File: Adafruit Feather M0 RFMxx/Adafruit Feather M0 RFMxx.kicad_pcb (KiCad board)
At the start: 2 copper layers, 50.8 x 22.9 mm, 41 parts, among them SW1 SPST_TACT-KMR2, U1 2MB Flash, U2 AP2112K-3.3, U3 MCP73831T-2ACI/OT, U4 RFM69HCW, X1 JSTPH, X2 32.768, X3 microUSB, X4 uFL

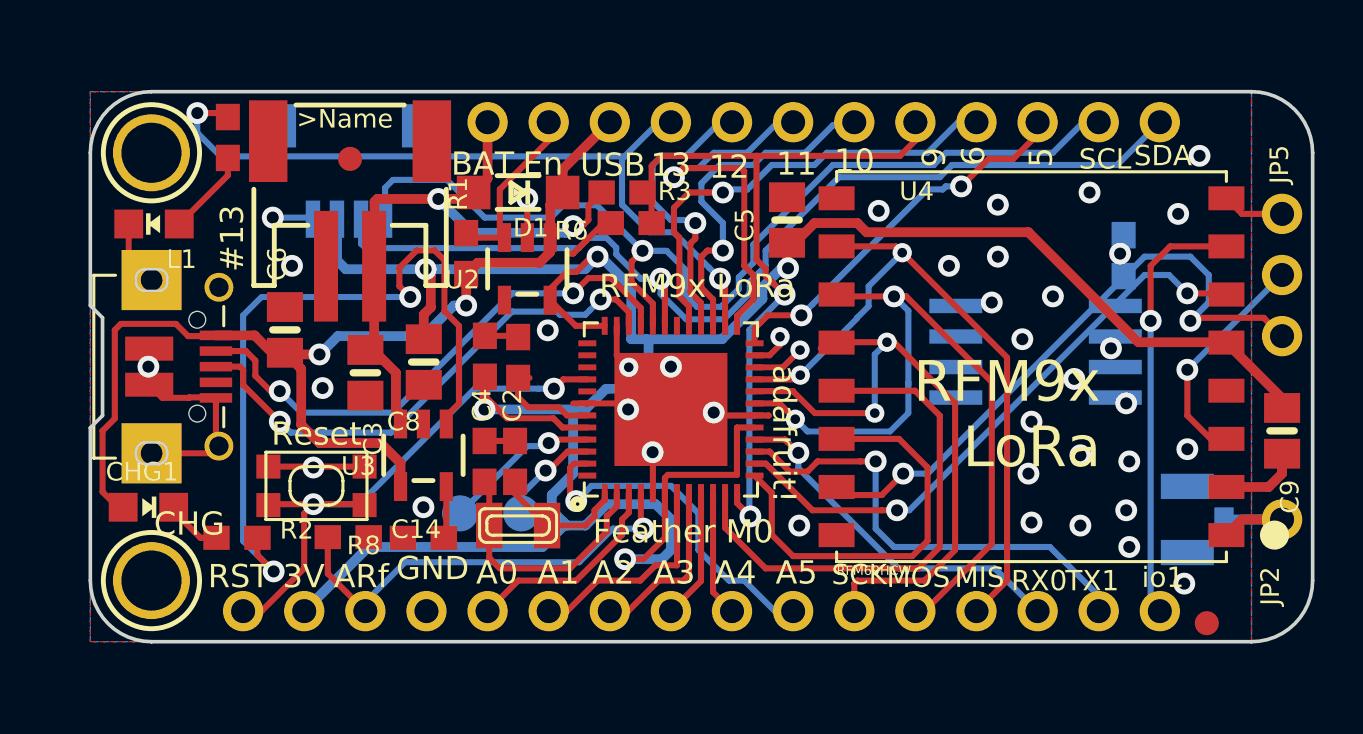
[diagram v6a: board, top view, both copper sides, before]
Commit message: New RST and IRQ lines chosen for RFM. Everything routed. DRC errors still to be fixed.
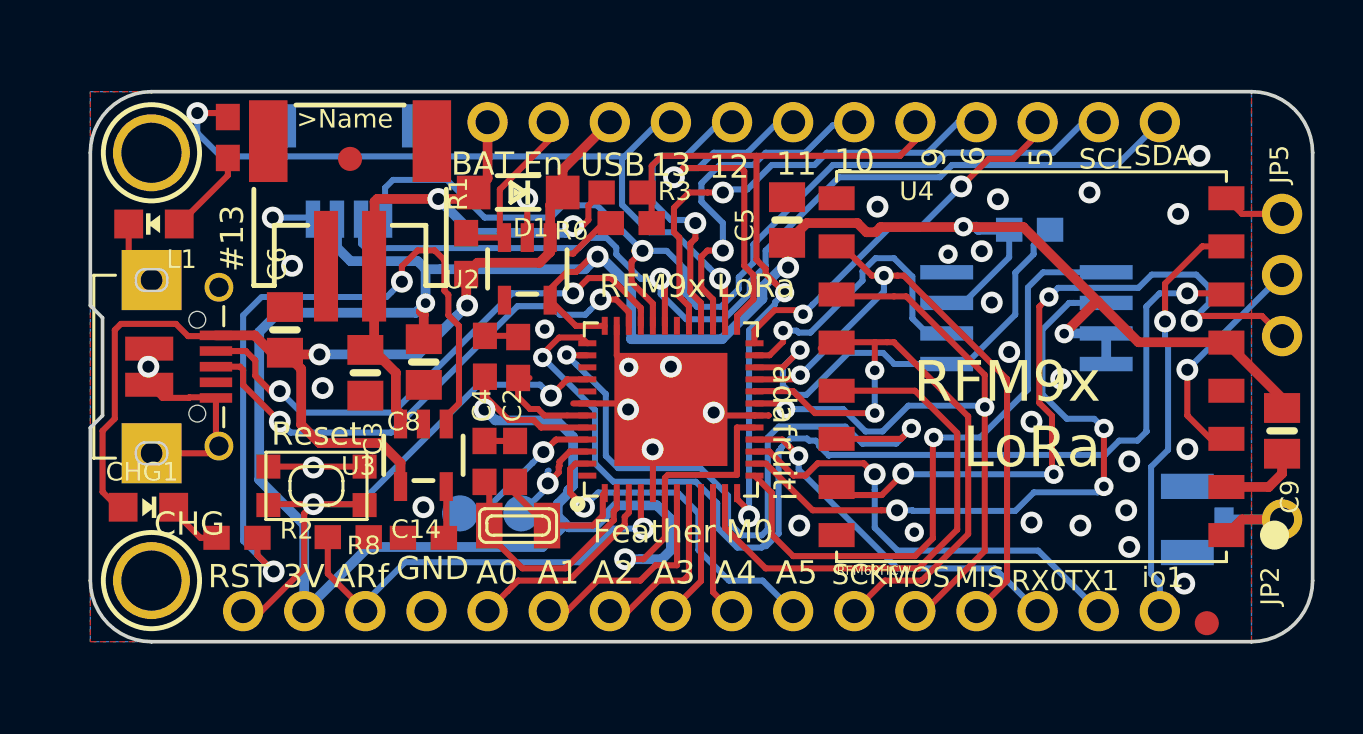
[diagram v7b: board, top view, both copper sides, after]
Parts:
- moved R4 4.05 mm to (162.1, 99.3), turned to 180 degrees
- moved U1 1.45 mm to (162.0, 103.0)
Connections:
- U$4 pad 13: /D4_RST -> /D4_FLASHMOSI
- U$4 pad 14: /D3_IRQ -> /D3_FLASHSCK
- U$4 pad 37: Net-(U$4-Pad37) -> /RXD_IRQ
- U$4 pad 38: Net-(U$4-Pad38) -> /TXD_RST
- U4 pad 14P: /D4_RST -> /TXD_RST
- U4 pad 6P: /D3_IRQ -> /RXD_IRQ
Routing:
- net /RXD_IRQ: track 0.00 -> 46.1 mm, vias 0 -> 2
- net /TXD_RST: track 0.00 -> 28.4 mm, vias 0 -> 2
- net /D4_FLASHMOSI: track 0.00 -> 27.6 mm, vias 0 -> 1
- net /D3_FLASHSCK: track 0.00 -> 27.1 mm, vias 0 -> 3
- net +3V3: track 112.8 -> 137.8 mm, vias 6 -> 7
- net /D3_IRQ: track 24.8 -> 0.00 mm, vias 2 -> 0
- net /FLASH_CS: track 2.19 -> 19.7 mm, vias 2 -> 1
- net /D4_RST: track 17.2 -> 0.00 mm
- net /D2_FLASHMISO: track 1.58 -> 12.5 mm
- net /DIO5: track 26.5 -> 30.5 mm, vias 2 -> 4
- net /MOSI: track 31.6 -> 29.3 mm
- net /MISO: track 28.9 -> 27.1 mm
- net Net-(R2-Pad2): track 31.0 -> 30.1 mm
- net /DIO1: track 18.0 -> 17.3 mm
- net Net-(C4-Pad1): track 10.7 -> 10.1 mm
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
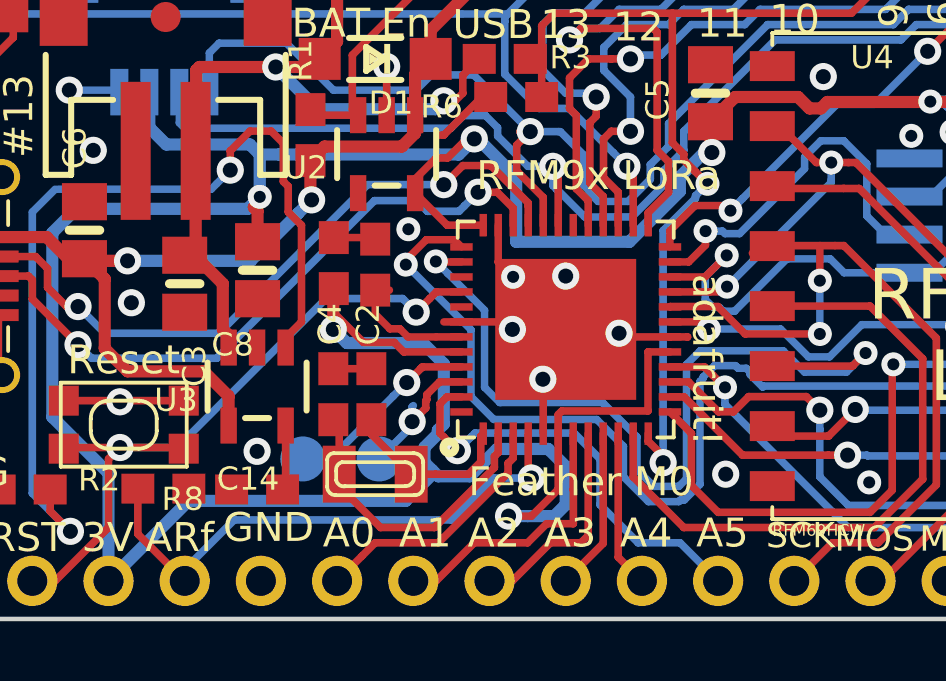
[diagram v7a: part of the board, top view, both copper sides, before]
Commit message: Fixed DRC errors. Remaining are ignores? - 2 pads part of USB connector - Top and Bottom regions not connected
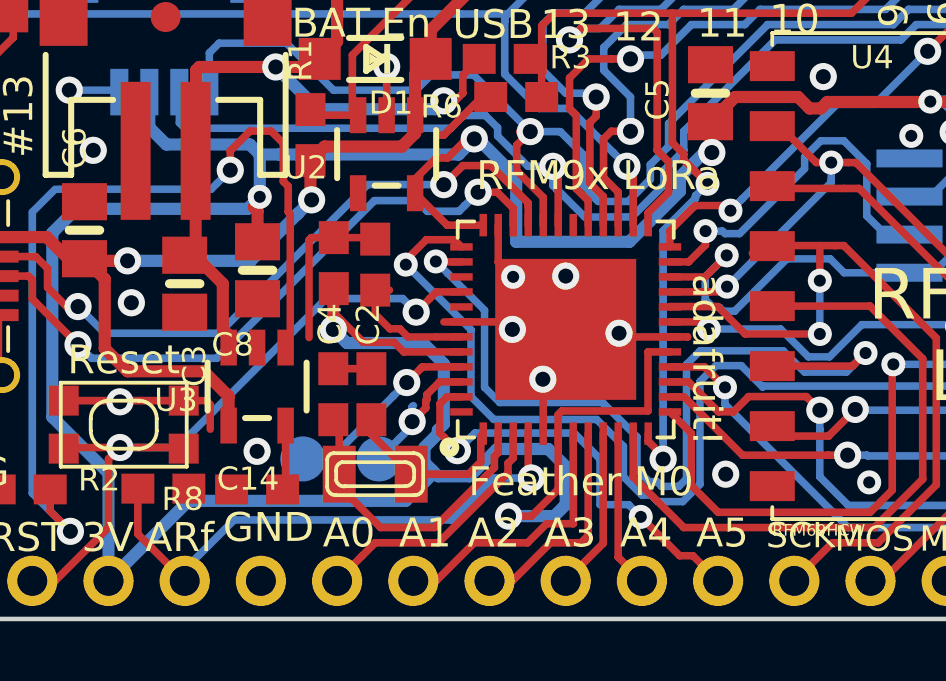
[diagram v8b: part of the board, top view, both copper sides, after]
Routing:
- net GND: track 44.9 -> 50.8 mm, vias 33 -> 32
- net /A5: vias 1 -> 2
